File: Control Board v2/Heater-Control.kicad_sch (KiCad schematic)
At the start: 11 parts, among them J2 1366005, U2 MOC3083S-TA1

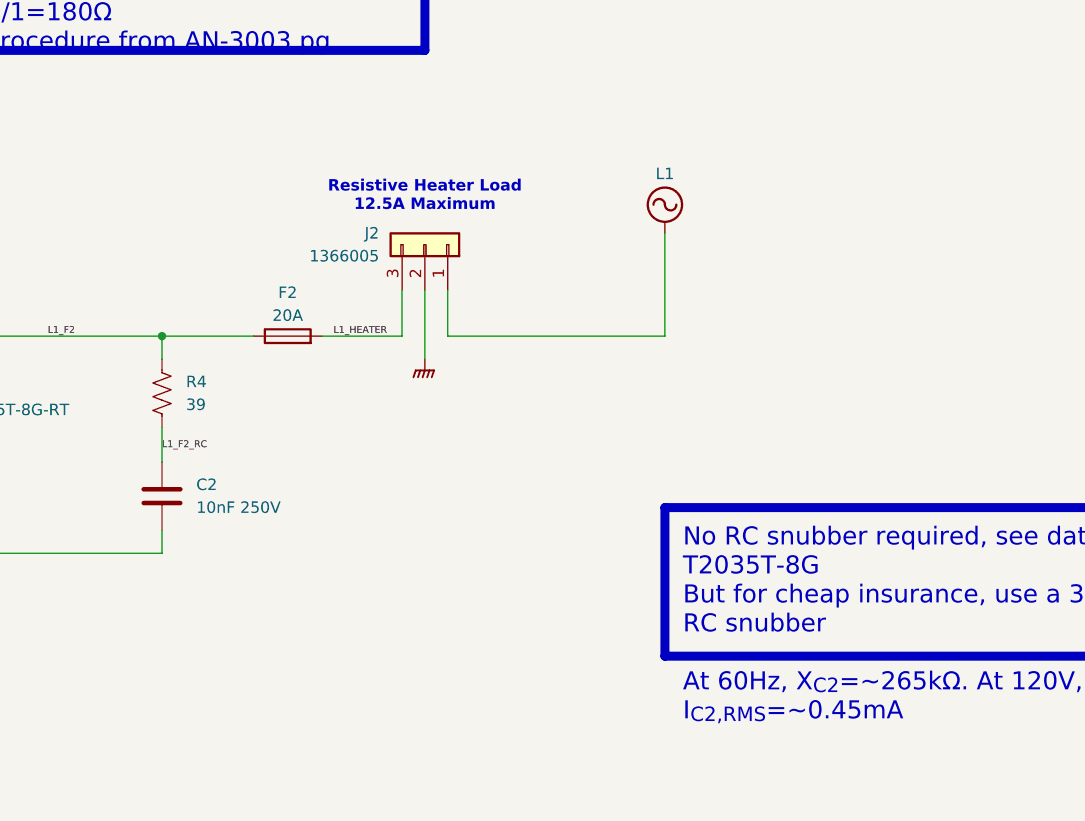
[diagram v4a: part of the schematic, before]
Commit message: got most HV routed
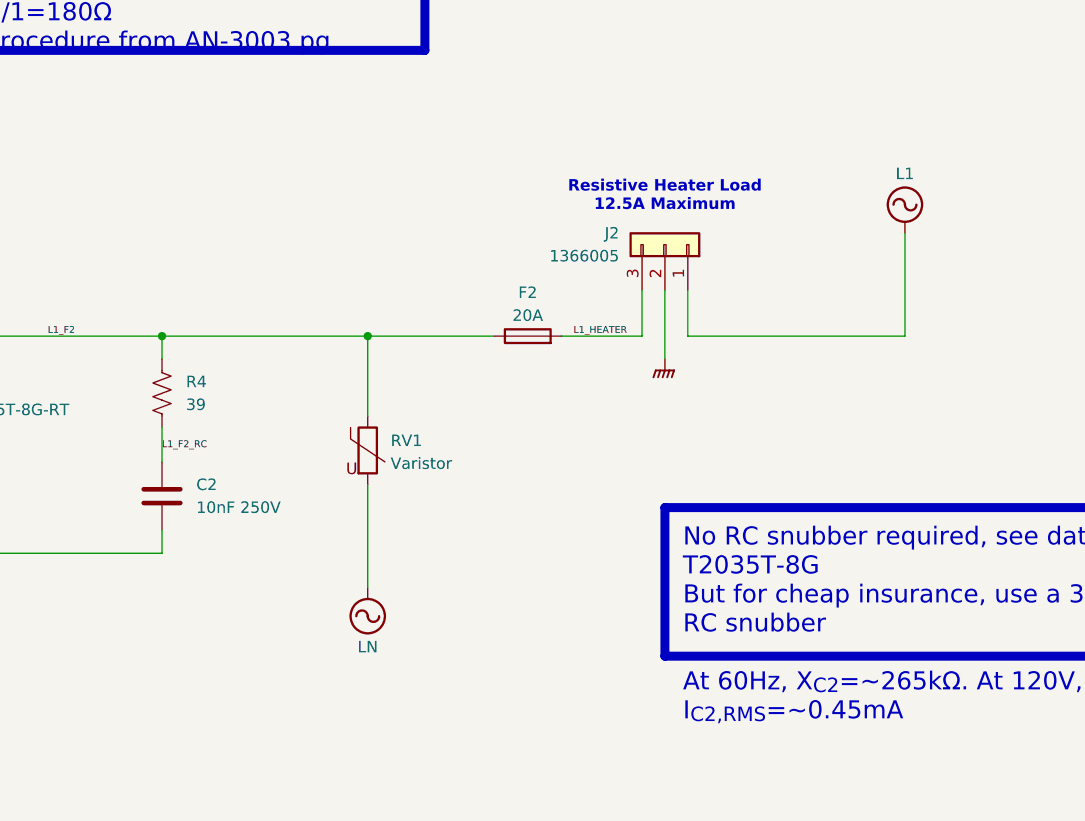
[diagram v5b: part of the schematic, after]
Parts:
- added RV1: Varistor, symbol Device:Varistor
- F2: footprint Fuse:Fuse_Blade_ATO_directSolder -> Fuse:Fuseholder_Clip-6.3x32mm_Littelfuse_122_Inline_P34.21x7.62mm_D2.54mm_Horizontal
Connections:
- net L1_F2: now also RV1.1
- net LN: now also RV1.2
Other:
- moved on the sheet: F2, J2
